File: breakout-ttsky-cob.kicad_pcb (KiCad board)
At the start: 4 copper layers, 50 x 50 mm, 124 parts, among them J1 DF12NB-60DS-0.5V_51, J2 Conn_01x12, J3 DF12NB-50DS-0.5V_51, U1 AP2112K-1.8, U2 AP2112K-1.8, U3 24LC02, U4 Openframe_QFN_TT06_REV2

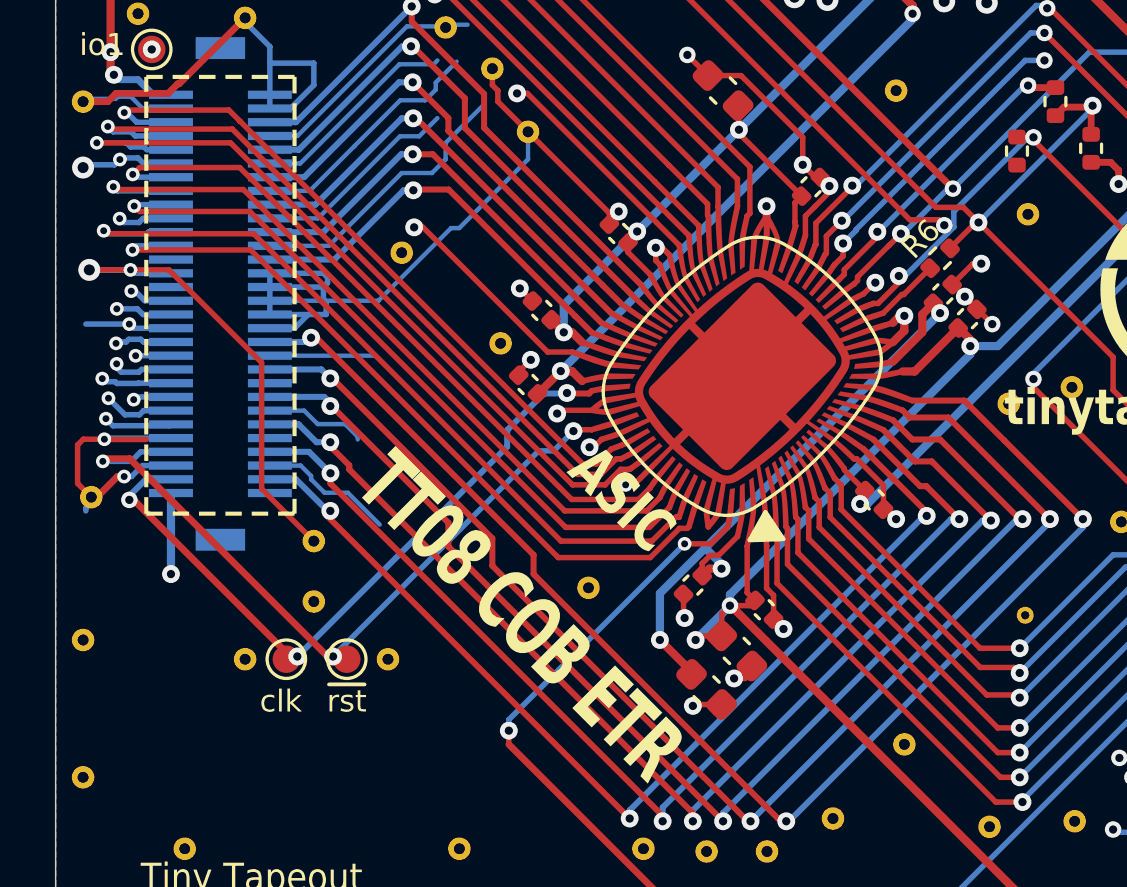
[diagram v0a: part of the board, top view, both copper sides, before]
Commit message: add extra ground & edit widths
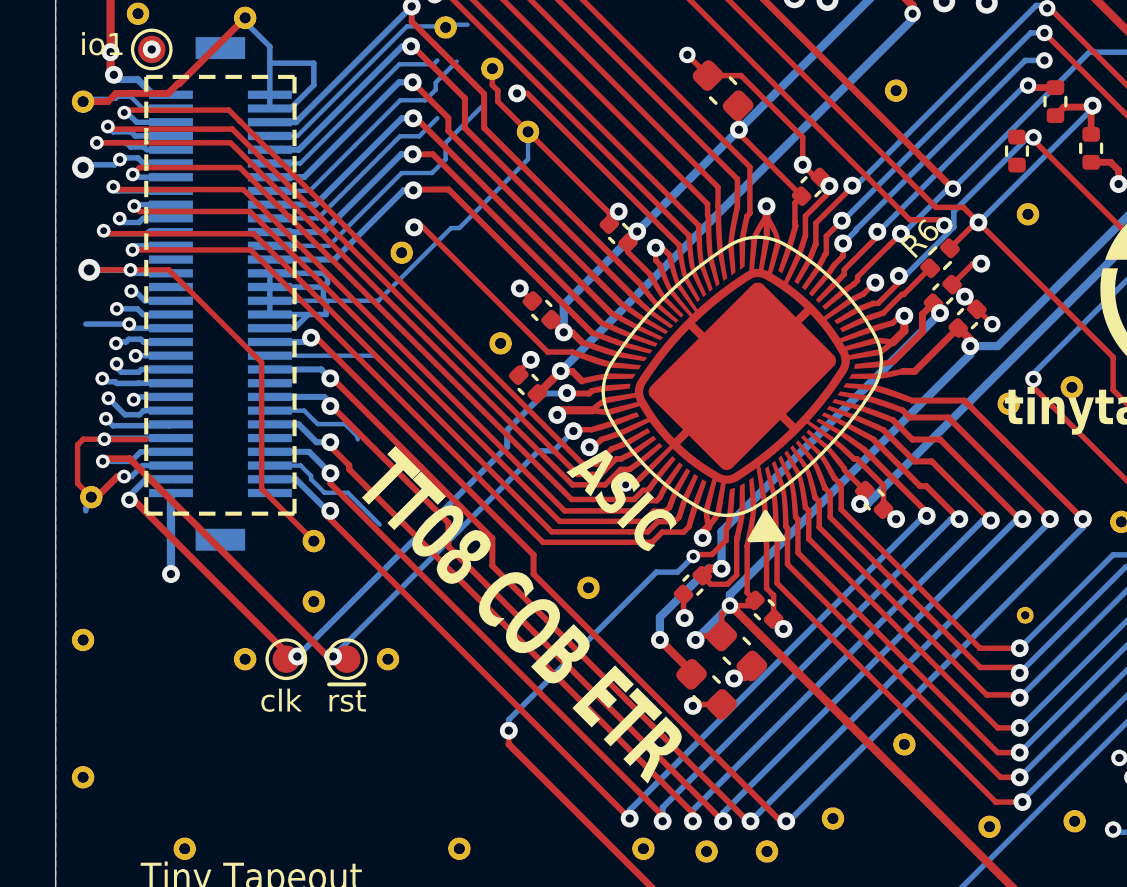
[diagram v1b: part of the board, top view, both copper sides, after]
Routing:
- net GND: track 302.9 -> 303.4 mm, vias 64 -> 65
